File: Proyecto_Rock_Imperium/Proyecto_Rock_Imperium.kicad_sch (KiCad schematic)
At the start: 15 parts, among them Q1 2N3904, Q2 2N3904

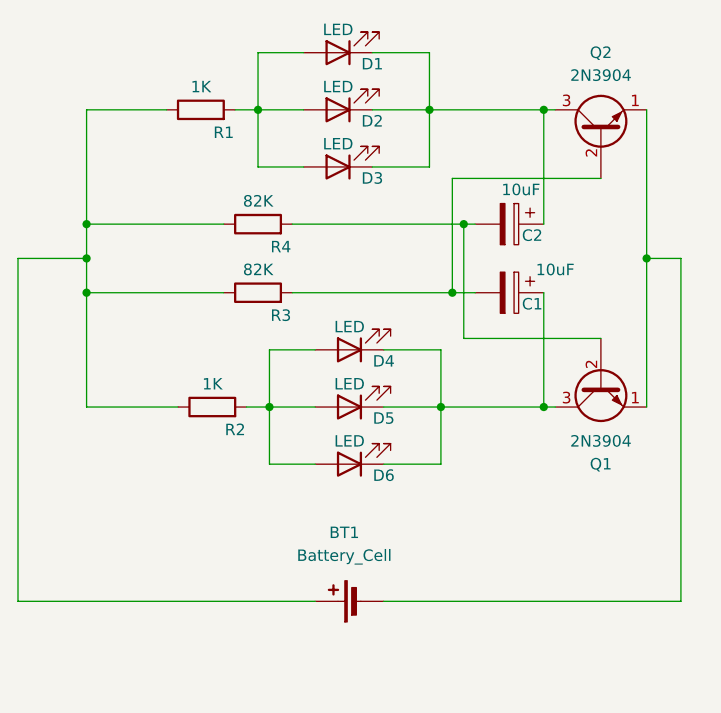
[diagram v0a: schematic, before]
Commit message: Actualizado esquema y añadido switch
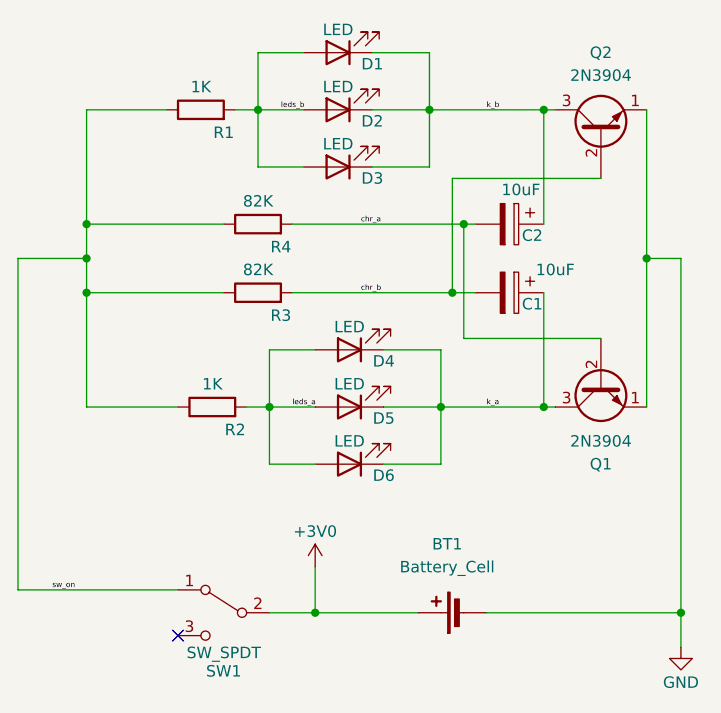
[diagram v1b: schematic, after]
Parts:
- added SW1: SW_SPDT, Button_Switch_SMD:SW_SPDT_PCM12, symbol Switch:SW_SPDT
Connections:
- net k_a: now reaches C1.1, D4.1 (K), D5.1 (K), D6.1 (K), Q1.3 (C)
- net leds_a: now reaches D4.2 (A), D5.2 (A), D6.2 (A), R2.2
- net k_b: now reaches C2.1, D1.1 (K), D2.1 (K), D3.1 (K), Q2.3 (C)
- net chr_a: now reaches C2.2, Q1.2 (B), R4.2
- net leds_b: now reaches D1.2 (A), D2.2 (A), D3.2 (A), R1.2
- net sw_on: now reaches R1.1, R2.1, R3.1, R4.1
- net sw_on: now also SW1.1 (A); no longer BT1.1 (+)
- net GND: now reaches BT1.2 (-), Q1.1 (E), Q2.1 (E)
- net chr_b: now reaches C1.2, Q2.2 (B), R3.2
- new net +3V0: BT1.1 (+), SW1.2 (B)
- no-connect marks 0 -> 1
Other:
- moved on the sheet: BT1
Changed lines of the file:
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@@
   (junction (at 173.99 71.12) (diameter 0) (color 0 0 0 0)
   )
+  (junction (at 148.59 127) (diameter 0) (color 0 0 0 0)
+  )
   (junction (at 161.29 71.12) (diameter 0) (color 0 0 0 0)
   )
@@
   (junction (at 123.19 87.63) (diameter 0) (color 0 0 0 0)
   )
+  (junction (at 189.23 127) (diameter 0) (color 0 0 0 0)
+  )
   (junction (at 163.83 91.44) (diameter 0) (color 0 0 0 0)
   )
   (junction (at 173.99 104.14) (diameter 0) (color 0 0 0 0)
   )
+  (no_connect (at 133.35 129.54))
   (wire (pts (xy 185.42 87.63) (xy 185.42 104.14))
     (stroke (width 0) (type default))
@@
     (stroke (width 0) (type default))
   )
-  (wire (pts (xy 189.23 125.73) (xy 189.23 87.63))
+  (wire (pts (xy 189.23 127) (xy 189.23 87.63))
     (stroke (width 0) (type default))
   )
@@
     (stroke (width 0) (type default))
   )
-  (wire (pts (xy 156.21 125.73) (xy 189.23 125.73))
+  (wire (pts (xy 167.64 127) (xy 189.23 127))
     (stroke (width 0) (type default))
   )
@@
     (stroke (width 0) (type default))
   )
+  (wire (pts (xy 148.59 127) (xy 160.02 127))
+    (stroke (width 0) (type default))
+  )
   (wire (pts (xy 148.59 97.79) (xy 143.51 97.79))
     (stroke (width 0) (type default))
   )
+  (wire (pts (xy 143.51 127) (xy 148.59 127))
+    (stroke (width 0) (type default))
+  )
   (wire (pts (xy 161.29 71.12) (xy 173.99 71.12))
     (stroke (width 0) (type default))
@@
     (stroke (width 0) (type default))
   )
-  (wire (pts (xy 148.59 125.73) (xy 115.57 125.73))
-    (stroke (width 0) (type default))
-  )
   (wire (pts (xy 142.24 77.47) (xy 147.32 77.47))
     (stroke (width 0) (type default))
   )
-  (wire (pts (xy 115.57 125.73) (xy 115.57 87.63))
+  (wire (pts (xy 115.57 124.46) (xy 133.35 124.46))
+    (stroke (width 0) (type default))
+  )
+  (wire (pts (xy 148.59 121.92) (xy 148.59 127))
+    (stroke (width 0) (type default))
+  )
+  (wire (pts (xy 115.57 124.46) (xy 115.57 87.63))
     (stroke (width 0) (type default))
   )
@@
     (stroke (width 0) (type default))
   )
+  (wire (pts (xy 189.23 127) (xy 189.23 130.81))
+    (stroke (width 0) (type default))
+  )
   (wire (pts (xy 142.24 71.12) (xy 142.24 77.47))
     (stroke (width 0) (type default))
@@
     (stroke (width 0) (type default))
   )
+  (label "leds_a" (at 146.05 104.14 0) (fields_autoplaced)
+    (effects (font (size 0.6 0.6)) (justify left bottom))
+  )
+  (label "chr_b" (at 153.67 91.44 0) (fields_autoplaced)
+    (effects (font (size 0.6 0.6)) (justify left bottom))
+  )
+  (label "sw_on" (at 119.38 124.46 0) (fields_autoplaced)
+    (effects (font (size 0.6 0.6)) (justify left bottom))
+  )
+  (label "chr_a" (at 153.67 83.82 0) (fields_autoplaced)
+    (effects (font (size 0.6 0.6)) (justify left bottom))
+  )
+  (label "k_a" (at 167.64 104.14 0) (fields_autoplaced)
+    (effects (font (size 0.6 0.6)) (justify left bottom))
+  )
+  (label "k_b" (at 167.64 71.12 0) (fields_autoplaced)
+    (effects (font (size 0.6 0.6)) (justify left bottom))
+  )
+  (label "leds_b" (at 144.78 71.12 0) (fields_autoplaced)
+    (effects (font (size 0.6 0.6)) (justify left bottom))
+  )
   (symbol (lib_id "Device:LED") (at 152.4 97.79 180) (unit 1)
     (in_bom yes) (on_board yes) (dnp no)
@@
     )
   )
+  (symbol (lib_id "power:GND") (at 189.23 130.81 0) (unit 1)
+    (in_bom yes) (on_board yes) (dnp no) (fields_autoplaced)
+    (property "Reference" "#PWR01" (at 189.23 137.16 0)
+      (effects (font (size 1.27 1.27)) hide)
+    )
+    (property "Value" "GND" (at 189.23 134.755 0)
+      (effects (font (size 1.27 1.27)))
+    )
+    (property "Footprint" "" (at 189.23 130.81 0)
+      (effects (font (size 1.27 1.27)) hide)
+    )
+    (property "Datasheet" "" (at 189.23 130.81 0)
+      (effects (font (size 1.27 1.27)) hide)
+    )
+    (pin "1")
+    (instances
+      (project "Proyecto_Rock_Imperium"
+        (path "/0d2850ca-6d2a-4d49-bcc8-777e40b8f294"
+          (reference "#PWR01") (unit 1)
+        )
+      )
+    )
+  )
   (symbol (lib_id "Device:C_Polarized") (at 170.18 83.82 270) (unit 1)
     (in_bom yes) (on_board yes) (dnp no)
@@
     )
   )
+  (symbol (lib_id "power:+3V0") (at 148.59 121.92 0) (unit 1)
+    (in_bom yes) (on_board yes) (dnp no) (fields_autoplaced)
+    (property "Reference" "#PWR02" (at 148.59 125.73 0)
+      (effects (font (size 1.27 1.27)) hide)
+    )
+    (property "Value" "+3V0" (at 148.59 117.975 0)
+      (effects (font (size 1.27 1.27)))
+    )
+    (property "Footprint" "" (at 148.59 121.92 0)
+      (effects (font (size 1.27 1.27)) hide)
+    )
+    (property "Datasheet" "" (at 148.59 121.92 0)
+      (effects (font (size 1.27 1.27)) hide)
+    )
+    (pin "1")
+    (instances
+      (project "Proyecto_Rock_Imperium"
+        (path "/0d2850ca-6d2a-4d49-bcc8-777e40b8f294"
+          (reference "#PWR02") (unit 1)
+        )
+      )
+    )
+  )
   (symbol (lib_id "Device:LED") (at 151.13 71.12 180) (unit 1)
     (in_bom yes) (on_board yes) (dnp no)
@@
     )
   )
-  (symbol (lib_id "Device:Battery_Cell") (at 153.67 125.73 90) (unit 1)
+  (symbol (lib_id "Device:Battery_Cell") (at 165.1 127 90) (unit 1)
     (in_bom yes) (on_board yes) (dnp no) (fields_autoplaced)
-    (property "Reference" "BT1" (at 151.8285 118.11 90)
-      (effects (font (size 1.27 1.27)))
-    )
-    (property "Value" "Battery_Cell" (at 151.8285 120.65 90)
-      (effects (font (size 1.27 1.27)))
-    )
-    (property "Footprint" "Battery:BatteryHolder_Keystone_3002_1x2032" (at 152.146 125.73 90)
-      (effects (font (size 1.27 1.27)) hide)
-    )
-    (property "Datasheet" "~" (at 152.146 125.73 90)
+    (property "Reference" "BT1" (at 163.2585 119.38 90)
+      (effects (font (size 1.27 1.27)))
+    )
+    (property "Value" "Battery_Cell" (at 163.2585 121.92 90)
+      (effects (font (size 1.27 1.27)))
+    )
+    (property "Footprint" "Battery:BatteryHolder_Keystone_3002_1x2032" (at 163.576 127 90)
+      (effects (font (size 1.27 1.27)) hide)
+    )
+    (property "Datasheet" "~" (at 163.576 127 90)
       (effects (font (size 1.27 1.27)) hide)
     )
@@
         )
       )
+    )
+  )
+  (symbol (lib_id "Switch:SW_SPDT") (at 138.43 127 0) (mirror y) (unit 1)
+    (in_bom yes) (on_board yes) (dnp no)
+    (property "Reference" "SW1" (at 138.43 133.501 0)
+      (effects (font (size 1.27 1.27)))
+    )
+    (property "Value" "SW_SPDT" (at 138.43 131.453 0)
+      (effects (font (size 1.27 1.27)))
+    )
+    (property "Footprint" "Button_Switch_SMD:SW_SPDT_PCM12" (at 138.43 127 0)
+      (effects (font (size 1.27 1.27)) hide)
+    )
+    (property "Datasheet" "~" (at 138.43 127 0)
+      (effects (font (size 1.27 1.27)) hide)
+    )
+    (pin "1")
+    (pin "2")
+    (pin "3")
+    (instances
+      (project "Proyecto_Rock_Imperium"
+        (path "/0d2850ca-6d2a-4d49-bcc8-777e40b8f294"
+          (reference "SW1") (unit 1)
+        )
+      )
